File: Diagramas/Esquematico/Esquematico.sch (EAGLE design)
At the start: 48 parts, among them IC1 RASPBERRY_PI_ZERO_W_(V1.3), IC2 3071, IC3 DS3231N_DIP, J1 Modulo Pir, K1 SRD-05VDC-SL-C, K2 SRD-05VDC-SL-C, K3 SRD-05VDC-SL-C, K4 SRD-05VDC-SL-C, U1 RFM69HW-868S2

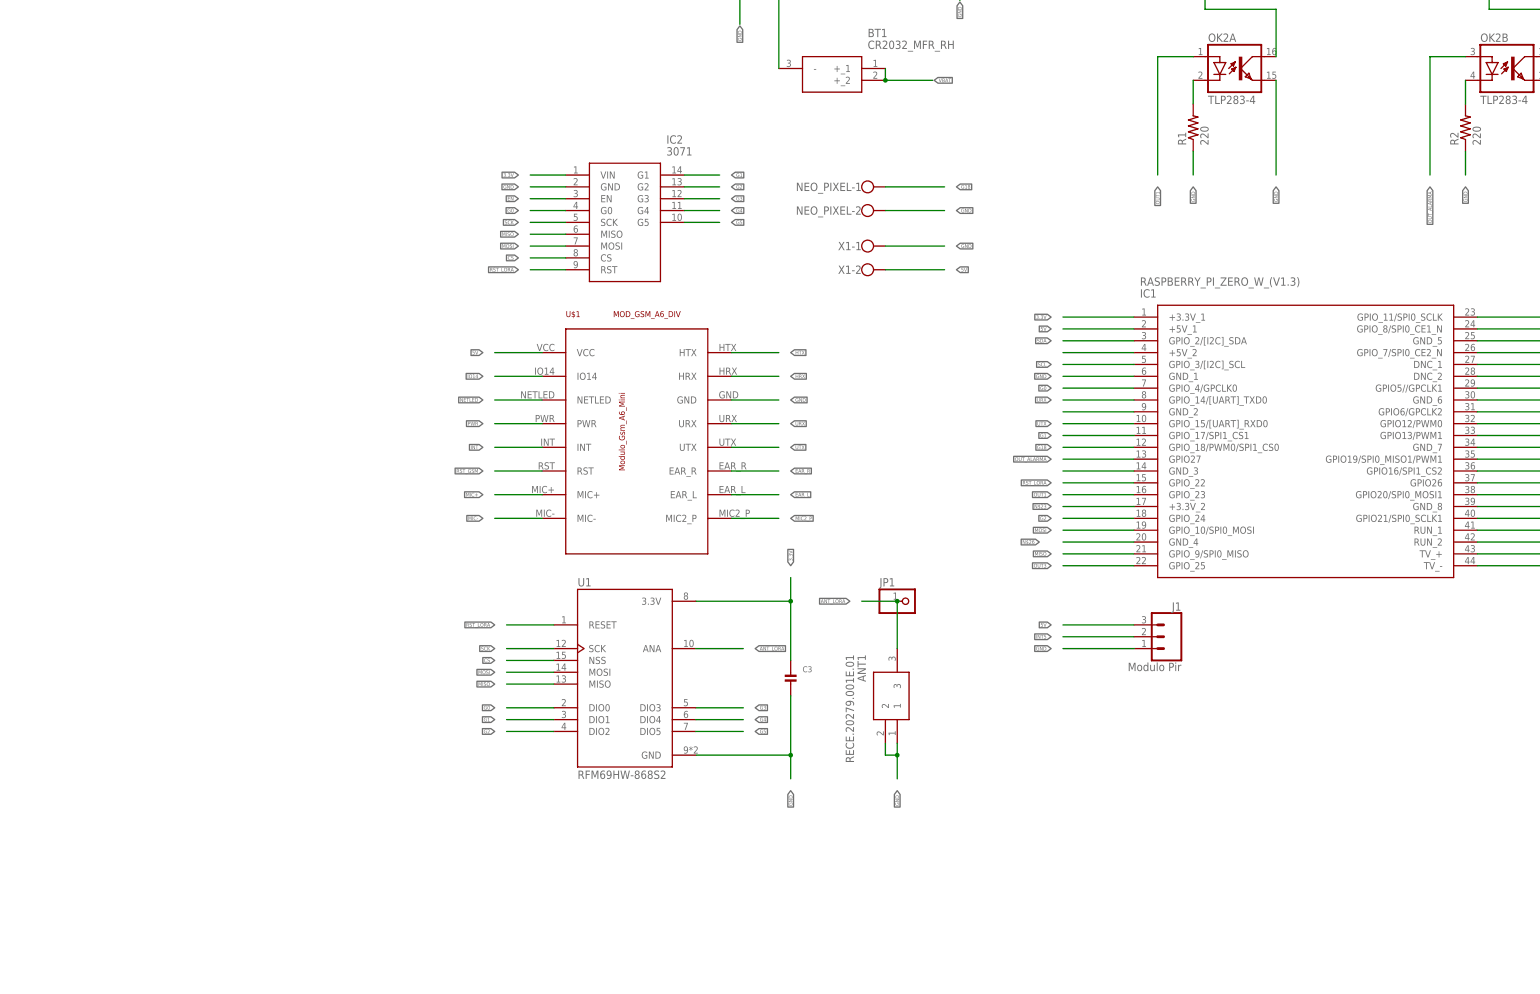
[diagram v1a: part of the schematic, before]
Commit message: Modulos en smd
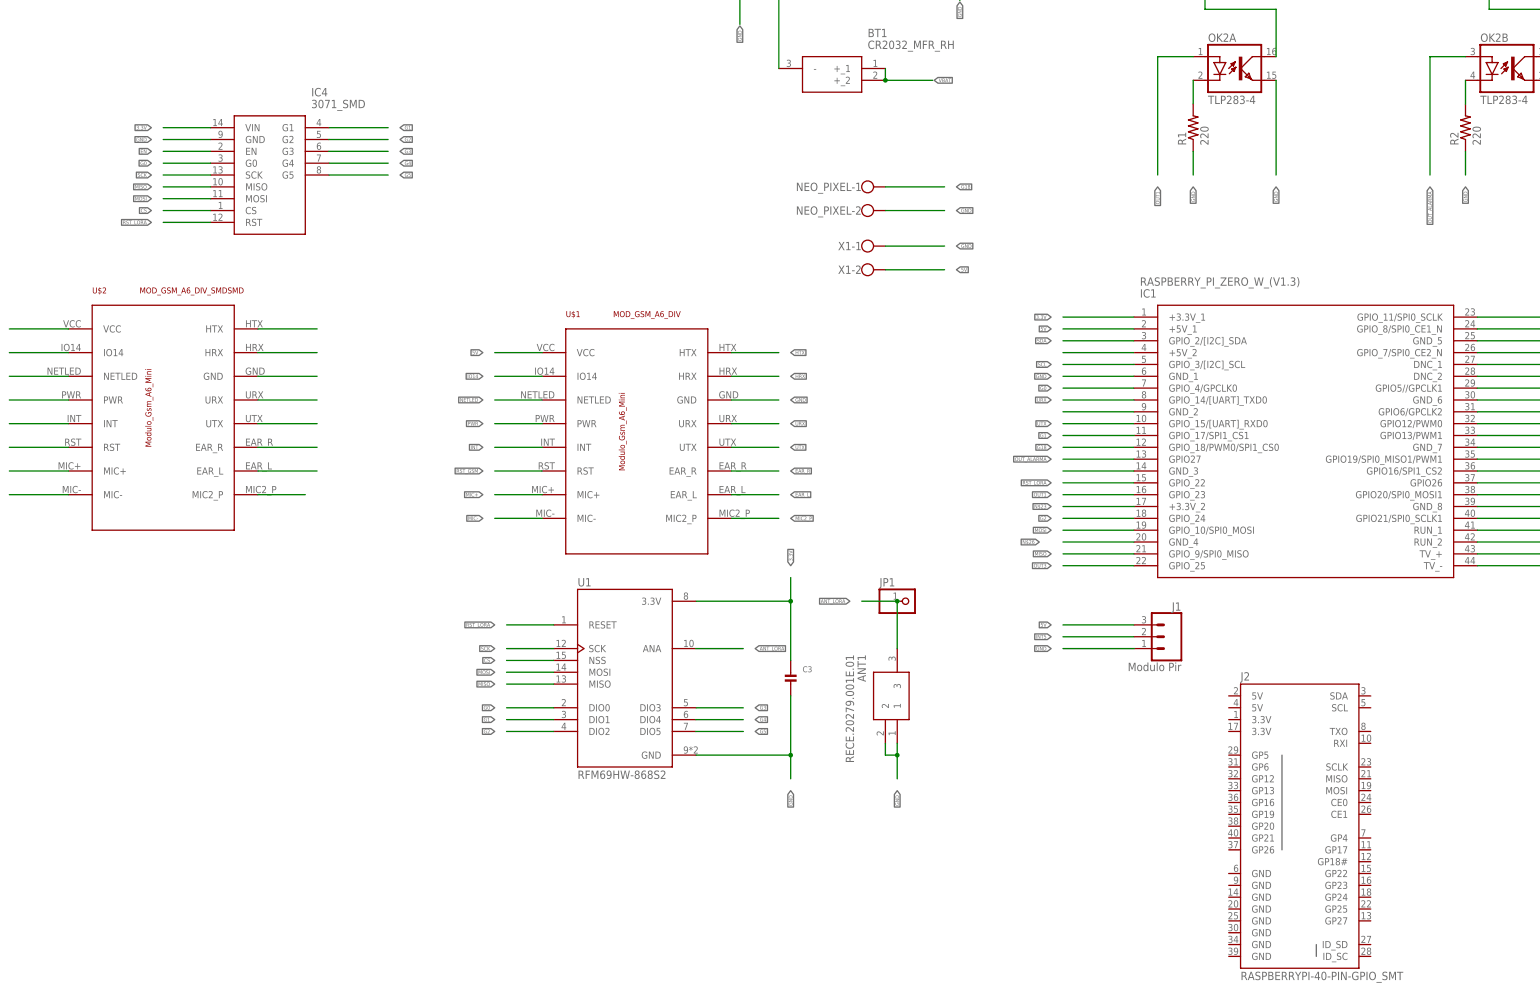
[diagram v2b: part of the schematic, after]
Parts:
- removed IC2: 3071, 3071:3071
- added IC4: 3071_SMD, 3071:3071_SMD
- added J2: RASPBERRYPI-40-PIN-GPIO_SMT, SparkFun-Connectors:RASPBERRYPI-40-PIN-GPIO_SMT
- added U$2: MOD_GSM_A6_DIV_SMDSMD, GPRS_A6 Mini:MOD_GSM_A6_DIV_SMDSMD
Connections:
- new net N$50: U$2.HTX
- new net N$51: U$2.HRX
- new net N$52: U$2.GND
- new net N$53: U$2.URX
- new net N$54: U$2.UTX
- new net N$55: U$2.EAR_R
- new net N$56: U$2.EAR_L
- new net N$57: U$2.MIC2_P
- new net N$58: U$2.VCC
- new net N$59: U$2.IO14
- new net N$60: U$2.NETLED
- new net N$61: U$2.PWR
- new net N$62: U$2.INT
- new net N$63: U$2.RST
- new net N$64: U$2.MIC+
- new net N$65: U$2.MIC-
- net 3.3V: now also IC4.VIN; no longer IC2.VIN
- net CS: now also IC4.CS; no longer IC2.CS
- net EN: now also IC4.EN; no longer IC2.EN
- net G0: now also IC4.G0; no longer IC2.G0
- net G1: now also IC4.G1; no longer IC2.G1
- net G2: now also IC4.G2; no longer IC2.G2
- net G3: now also IC4.G3; no longer IC2.G3
- net G4: now also IC4.G4; no longer IC2.G4
- net G5: now also IC4.G5; no longer IC2.G5
- net GND: now also IC4.GND; no longer IC2.GND
- net MISO: now also IC4.MISO; no longer IC2.MISO
- net MOSI: now also IC4.MOSI; no longer IC2.MOSI
- net RST_LORA: now also IC4.RST; no longer IC2.RST
- net SCK: now also IC4.SCK; no longer IC2.SCK

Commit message: Acomo de coponentes
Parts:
- removed BT1: CR2032_MFR_RH, CR2032_MFR_RH:CR2032_MFR_RH
- removed IC1: RASPBERRY_PI_ZERO_W_(V1.3), Raspberry_Pi_Zero_W_(v1.3):RASPBERRY_PI_ZERO_W_(V1.3)
- removed U$1: MOD_GSM_A6_DIV, GPRS_A6 Mini:MOD_GSM_A6_DIV
- added BT2: BU2032SM-BT-GTR, BU2032SM-BT-GTR:BU2032SM-BT-GTR
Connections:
- removed net N$2: IC1.+5V_2
- removed net N$22: IC1.GND_3
- removed net N$23: IC1.+3.3V_2
- removed net N$26: IC1.GND_4
- removed net N$29: IC1.GND_5
- removed net N$36: IC1.DNC_1
- removed net N$37: IC1.DNC_2
- removed net N$38: IC1.GND_6
- removed net N$40: IC1.GND_7
- removed net N$41: IC1.GPIO16/SPI1_CS2
- removed net N$42: IC1.GPIO20/SPI0_MOSI1
- removed net N$43: IC1.GND_8
- removed net N$44: IC1.GPIO21/SPI0_SCLK1
- removed net N$45: IC1.RUN_1
- removed net N$46: IC1.RUN_2
- removed net N$47: IC1.TV_+
- removed net N$48: IC1.TV_-
- removed net N$57: U$2.MIC2_P
- removed net N$58: U$2.VCC
- removed net N$59: U$2.IO14
- removed net N$60: U$2.NETLED
- removed net N$61: U$2.PWR
- removed net N$62: U$2.INT
- removed net N$63: U$2.RST
- removed net N$64: U$2.MIC+
- removed net N$65: U$2.MIC-
- removed net N$7: IC1.GND_2
- new net N$14: J2.3.3V@17
- new net N$25: J2.GP16
- new net N$30: J2.GP20
- new net N$31: J2.GP21
- new net N$6: J2.5V@4
- net 3.3V: now also J2.3.3V@1; no longer IC1.+3.3V_1
- net 5V: now also J2.5V@2, U$2.VCC; no longer IC1.+5V_1, U$1.VCC
- net EAR_L: now also U$2.EAR_L; no longer U$1.EAR_L
- net EAR_R: now also U$2.EAR_R; no longer U$1.EAR_R
- net EN: now also J2.CE0; no longer IC1.GPIO_8/SPI0_CE1_N
- net G0: now also J2.GP4; no longer IC1.GPIO_4/GPCLK0
- net G1: now also J2.GP17; no longer IC1.GPIO_17/SPI1_CS1
- net G18: now also J2.GP18#; no longer IC1.GPIO_18/PWM0/SPI1_CS0
- net G2: now also J2.GP24; no longer IC1.GPIO_24
- net G3: now also J2.CE1; no longer IC1.GPIO_7/SPI0_CE2_N
- net GND: now also BT2.-, J2.GND@6, U$2.GND; no longer BT1.-, IC1.GND_1, U$1.GND
- net HRX: now also U$2.HRX; no longer U$1.HRX
- net HTX: now also U$2.HTX; no longer U$1.HTX
- net INT: now also U$2.INT; no longer U$1.INT
- net INT1: now also J2.GP5; no longer IC1.GPIO5//GPCLK1
- net INT2: now also J2.GP12; no longer IC1.GPIO12/PWM0
- net INT3: now also J2.GP13; no longer IC1.GPIO13/PWM1
- net INT4: now also J2.GP19; no longer IC1.GPIO19/SPI0_MISO1/PWM1
- net INT5: now also J2.GP26; no longer IC1.GPIO26
- net IO14: now also U$2.IO14; no longer U$1.IO14
- net MIC+: now also U$2.MIC+; no longer U$1.MIC+
- net MIC-: now also U$2.MIC-; no longer U$1.MIC-
- net MIC2_P: now also U$2.MIC2_P; no longer U$1.MIC2_P
- net MISO: now also J2.MISO; no longer IC1.GPIO_9/SPI0_MISO
- net MOSI: now also J2.MOSI; no longer IC1.GPIO_10/SPI0_MOSI
- net N$50: now also J2.GND@9; no longer U$2.HTX
- net N$51: now also J2.GND@14; no longer U$2.HRX
- net N$52: now also J2.GND@20; no longer U$2.GND
- net N$53: now also J2.GND@25; no longer U$2.URX
- net N$54: now also J2.GND@30; no longer U$2.UTX
- net N$55: now also J2.GND@34; no longer U$2.EAR_R
- net N$56: now also J2.GND@39; no longer U$2.EAR_L
- net NETLED: now also U$2.NETLED; no longer U$1.NETLED
- net OUT1: now also J2.GP23; no longer IC1.GPIO_23
- net OUT3: now also J2.GP25; no longer IC1.GPIO_25
- net OUT4: now also J2.GP6; no longer IC1.GPIO6/GPCLK2
- net OUT_ALARMA: now also J2.GP27; no longer IC1.GPIO27
- net PWR: now also U$2.PWR; no longer U$1.PWR
- net RST_GSM: now also U$2.RST; no longer U$1.RST
- net RST_LORA: now also J2.GP22; no longer IC1.GPIO_22
- net SCK: now also J2.SCLK; no longer IC1.GPIO_11/SPI0_SCLK
- net SCL: now also J2.SCL; no longer IC1.GPIO_3/[I2C]_SCL
- net SDA: now also J2.SDA; no longer IC1.GPIO_2/[I2C]_SDA
- net URX: now also J2.TXO, U$2.URX; no longer IC1.GPIO_14/[UART]_TXD0, U$1.URX
- net UTX: now also J2.RXI, U$2.UTX; no longer IC1.GPIO_15/[UART]_RXD0, U$1.UTX
- net VBAT: now also BT2.+; no longer BT1.+_1, BT1.+_2
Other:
- moved on the sheet: IC4, J2, U$2

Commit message: Ruteado de los componentes
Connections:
- net 5V: now also J1.2; no longer J1.3
- net INT5: now also J1.3; no longer J1.2
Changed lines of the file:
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@@
 <setting verticaltext="up"/>
 </settings>
-<grid distance="0.1" unitdist="inch" unit="mm" style="dots" multiple="1" display="yes" altdistance="0.01" altunitdist="inch" altunit="mm"/>
+<grid distance="0.1" unitdist="inch" unit="inch" style="lines" multiple="1" display="no" altdistance="0.01" altunitdist="inch" altunit="inch"/>
 <layers>
 <layer number="1" name="Top" color="4" fill="1" visible="no" active="no"/>
@@
 </segment>
 <segment>
-<pinref part="J1" gate="J$1" pin="3"/>
-<wire x1="-40.64" y1="127" x2="-55.88" y2="127" width="0.1524" layer="91"/>
-<label x="-58.42" y="127" size="0.8128" layer="95" rot="R180" xref="yes"/>
-</segment>
-<segment>
 <pinref part="X1" gate="-2" pin="KL"/>
 <wire x1="-93.98" y1="203.2" x2="-81.28" y2="203.2" width="0.1524" layer="91"/>
@@
 <wire x1="-25.4" y1="200.66" x2="-38.1" y2="200.66" width="0.1524" layer="91"/>
 <label x="-40.64" y="200.66" size="0.8128" layer="95" rot="R180" xref="yes"/>
+</segment>
+<segment>
+<pinref part="J1" gate="J$1" pin="2"/>
+<wire x1="-40.64" y1="124.46" x2="-55.88" y2="124.46" width="0.1524" layer="91"/>
+<label x="-58.42" y="124.46" size="0.8128" layer="95" rot="R180" xref="yes"/>
 </segment>
 </net>
@@
 <net name="INT5" class="0">
 <segment>
-<pinref part="J1" gate="J$1" pin="2"/>
-<wire x1="-40.64" y1="124.46" x2="-55.88" y2="124.46" width="0.1524" layer="91"/>
-<label x="-58.42" y="124.46" size="0.8128" layer="95" rot="R180" xref="yes"/>
-</segment>
-<segment>
 <pinref part="J2" gate="G$1" pin="GP26"/>
 <wire x1="-25.4" y1="167.64" x2="-38.1" y2="167.64" width="0.1524" layer="91"/>
 <label x="-40.64" y="167.64" size="0.8128" layer="95" rot="R180" xref="yes"/>
 </segment>
-</net>
+<segment>
+<pinref part="J1" gate="J$1" pin="3"/>
+<wire x1="-40.64" y1="127" x2="-55.88" y2="127" width="0.1524" layer="91"/>
+<label x="-58.42" y="127" size="0.8128" layer="95" rot="R180" xref="yes"/>
+</segment>
+</net>

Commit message: imagenes pcb
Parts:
- renumbered X1 to PWR
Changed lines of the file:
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@@
 <part name="INT3" library="con-wago-500" library_urn="urn:adsk.eagle:library:195" deviceset="W237-102" device="" package3d_urn="urn:adsk.eagle:package:10688/1"/>
 <part name="INT4" library="con-wago-500" library_urn="urn:adsk.eagle:library:195" deviceset="W237-102" device="" package3d_urn="urn:adsk.eagle:package:10688/1"/>
-<part name="X1" library="con-wago-500" library_urn="urn:adsk.eagle:library:195" deviceset="W237-102" device="" package3d_urn="urn:adsk.eagle:package:10688/1"/>
+<part name="PWR" library="con-wago-500" library_urn="urn:adsk.eagle:library:195" deviceset="W237-102" device="" package3d_urn="urn:adsk.eagle:package:10688/1"/>
 <part name="U1" library="RFM69HW-868S2" deviceset="RFM69HW-868S2" device=""/>
 <part name="JP1" library="microbuilder" deviceset="HEADER-1X1" device=""/>
@@
 <attribute name="NAME" x="83.82" y="112.649" size="1.778" layer="95" rot="R180"/>
 </instance>
-<instance part="X1" gate="-1" x="-99.06" y="208.28" smashed="yes">
+<instance part="PWR" gate="-1" x="-99.06" y="208.28" smashed="yes">
 <attribute name="NAME" x="-99.06" y="209.169" size="1.778" layer="95" rot="R180"/>
 </instance>
-<instance part="X1" gate="-2" x="-99.06" y="203.2" smashed="yes">
+<instance part="PWR" gate="-2" x="-99.06" y="203.2" smashed="yes">
 <attribute name="VALUE" x="-101.6" y="199.517" size="1.778" layer="96"/>
 <attribute name="NAME" x="-99.06" y="204.089" size="1.778" layer="95" rot="R180"/>
@@
 </segment>
 <segment>
-<pinref part="X1" gate="-1" pin="KL"/>
+<pinref part="PWR" gate="-1" pin="KL"/>
 <wire x1="-93.98" y1="208.28" x2="-81.28" y2="208.28" width="0.1524" layer="91"/>
 <label x="-78.74" y="208.28" size="0.8128" layer="95" xref="yes"/>
@@
 </segment>
 <segment>
-<pinref part="X1" gate="-2" pin="KL"/>
+<pinref part="PWR" gate="-2" pin="KL"/>
 <wire x1="-93.98" y1="203.2" x2="-81.28" y2="203.2" width="0.1524" layer="91"/>
 <label x="-78.74" y="203.2" size="0.8128" layer="95" xref="yes"/>
